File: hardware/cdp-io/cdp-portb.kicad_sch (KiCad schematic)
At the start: 5 parts, among them U1 74LS573, U2 74LS573, U7 74LS00

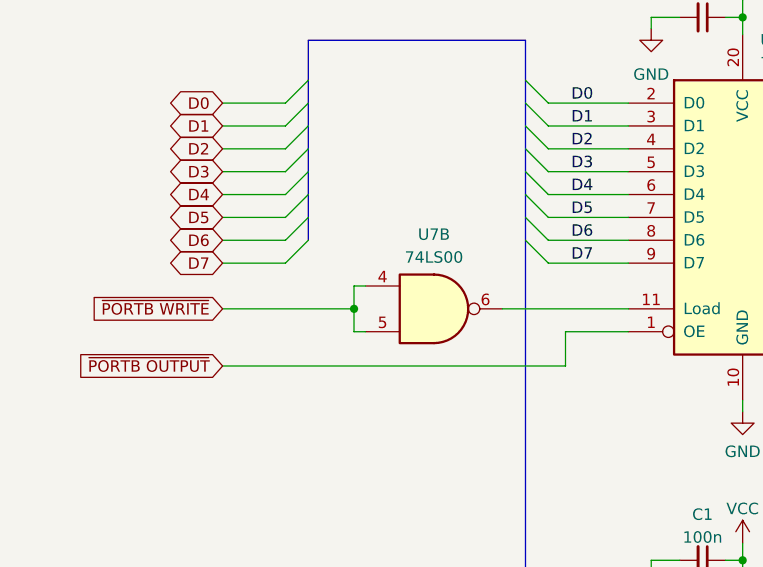
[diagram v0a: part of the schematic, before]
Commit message: The controller is finished. U7 is changed to a hex inverter.
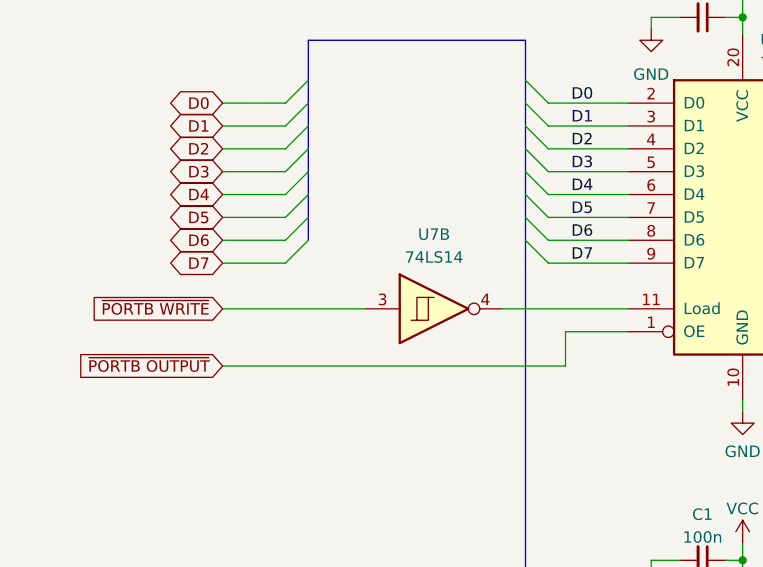
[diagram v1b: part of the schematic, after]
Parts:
- removed U7: 74LS00, Package_DIP:DIP-14_W7.62mm_Socket, symbol 74xx:74LS00
- added U7: 74LS14, symbol 74xx:74LS14
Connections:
- net ~{PORTB WRITE}: now also U7.3
- net at U1.11 (Load): now also U7.4
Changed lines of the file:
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@@
   (junction (at 155.575 93.345) (diameter 0) (color 0 0 0 0)
   )
-  (junction (at 112.395 65.405) (diameter 0) (color 0 0 0 0)
-  )
   (bus_entry (at 181.61 107.95) (size -2.54 2.54)
     (stroke (width 0) (type default))
@@
     (stroke (width 0) (type default))
   )
-  (wire (pts (xy 112.395 62.865) (xy 112.395 65.405))
-    (stroke (width 0) (type default))
-  )
   (wire (pts (xy 168.275 50.165) (xy 179.07 50.165))
     (stroke (width 0) (type default))
@@
     (stroke (width 0) (type default))
   )
-  (wire (pts (xy 112.395 65.405) (xy 112.395 67.945))
-    (stroke (width 0) (type default))
-  )
   (bus (pts (xy 206.375 55.245) (xy 206.375 57.785))
     (stroke (width 0) (type default))
@@
     (stroke (width 0) (type default))
   )
-  (wire (pts (xy 97.79 65.405) (xy 112.395 65.405))
+  (wire (pts (xy 97.79 65.405) (xy 113.665 65.405))
     (stroke (width 0) (type default))
   )
@@
     (stroke (width 0) (type default))
   )
-  (wire (pts (xy 112.395 67.945) (xy 113.665 67.945))
-    (stroke (width 0) (type default))
-  )
   (bus (pts (xy 181.61 42.545) (xy 181.61 40.005))
     (stroke (width 0) (type default))
@@
   )
   (wire (pts (xy 208.915 50.165) (xy 216.535 50.165))
-    (stroke (width 0) (type default))
-  )
-  (wire (pts (xy 113.665 62.865) (xy 112.395 62.865))
     (stroke (width 0) (type default))
   )
@@
     )
   )
-  (symbol (lib_id "74xx:74LS00") (at 121.285 65.405 0) (unit 2)
+  (symbol (lib_id "74xx:74LS14") (at 121.285 65.405 0) (unit 2)
     (in_bom yes) (on_board yes) (dnp no) (fields_autoplaced)
-    (property "Reference" "U7" (at 121.2767 57.15 0)
+    (property "Reference" "U7" (at 121.285 57.15 0)
       (effects (font (size 1.27 1.27)))
     )
-    (property "Value" "74LS00" (at 121.2767 59.69 0)
+    (property "Value" "74LS14" (at 121.285 59.69 0)
       (effects (font (size 1.27 1.27)))
     )
-    (property "Footprint" "Package_DIP:DIP-14_W7.62mm_Socket" (at 121.285 65.405 0)
-      (effects (font (size 1.27 1.27)) hide)
-    )
-    (property "Datasheet" "http://www.ti.com/lit/gpn/sn74ls00" (at 121.285 65.405 0)
+    (property "Footprint" "" (at 121.285 65.405 0)
+      (effects (font (size 1.27 1.27)) hide)
+    )
+    (property "Datasheet" "http://www.ti.com/lit/gpn/sn74LS14" (at 121.285 65.405 0)
       (effects (font (size 1.27 1.27)) hide)
     )
@@
     (pin "5")
     (pin "6")
-    (pin "10")
     (pin "8")
     (pin "9")
+    (pin "10")
     (pin "11")
     (pin "12")
@@
     (instances
       (project "cdp-io"
+        (path "/479e9a3e-8705-41df-8009-7e8503809f49/fc5dd19a-450f-4ce7-af21-025e7154e993"
+          (reference "U7") (unit 2)
+        )
         (path "/479e9a3e-8705-41df-8009-7e8503809f49/f2f2e87f-81b0-49e1-b285-4bb1f98f04a0"
           (reference "U7") (unit 2)

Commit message: Changed the layout a bit, started to work on the PCB.
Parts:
- U7: footprint (none) -> Package_DIP:DIP-14_W7.62mm_Socket
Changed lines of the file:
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@@
       (effects (font (size 1.27 1.27)))
     )
-    (property "Footprint" "" (at 121.285 65.405 0)
+    (property "Footprint" "Package_DIP:DIP-14_W7.62mm_Socket" (at 121.285 65.405 0)
       (effects (font (size 1.27 1.27)) hide)
     )

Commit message: Changed the schematic a bit.
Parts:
- removed U7: 74LS14, Package_DIP:DIP-14_W7.62mm_Socket, symbol 74xx:74LS14
- added U7: 74LS14, Package_DIP:DIP-14_W7.62mm_Socket, symbol 74xx:74LS14
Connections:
- net ~{PORTB WRITE}: now also U7.11
- net at U1.11 (Load): now also U7.10

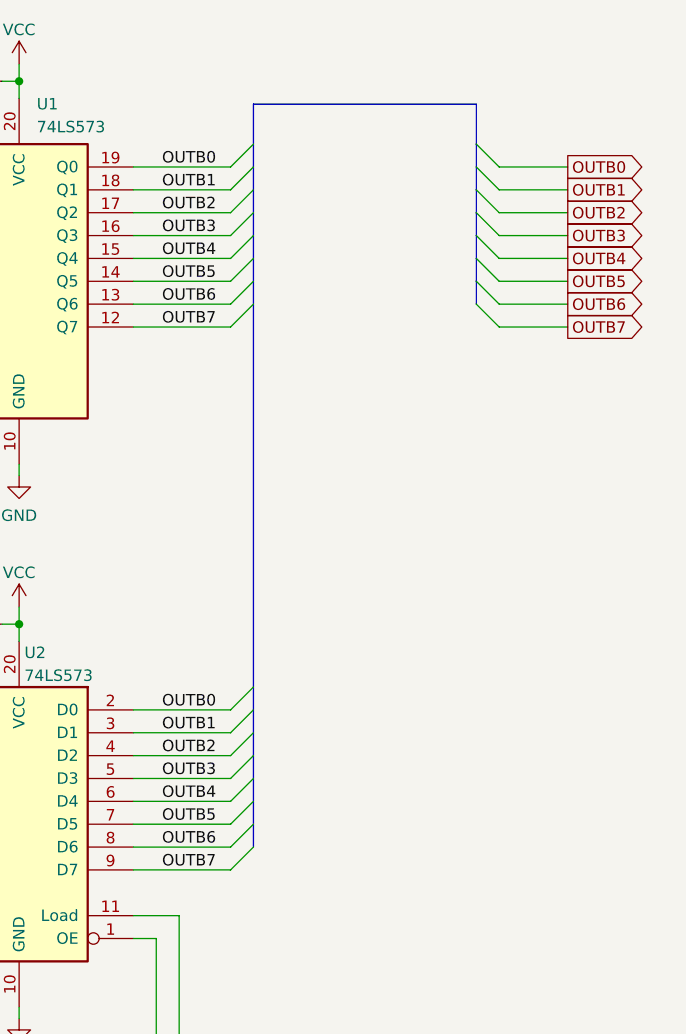
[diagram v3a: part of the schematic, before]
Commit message: Renamed a few net, and changed the schematic a bit. The PCB is ready!
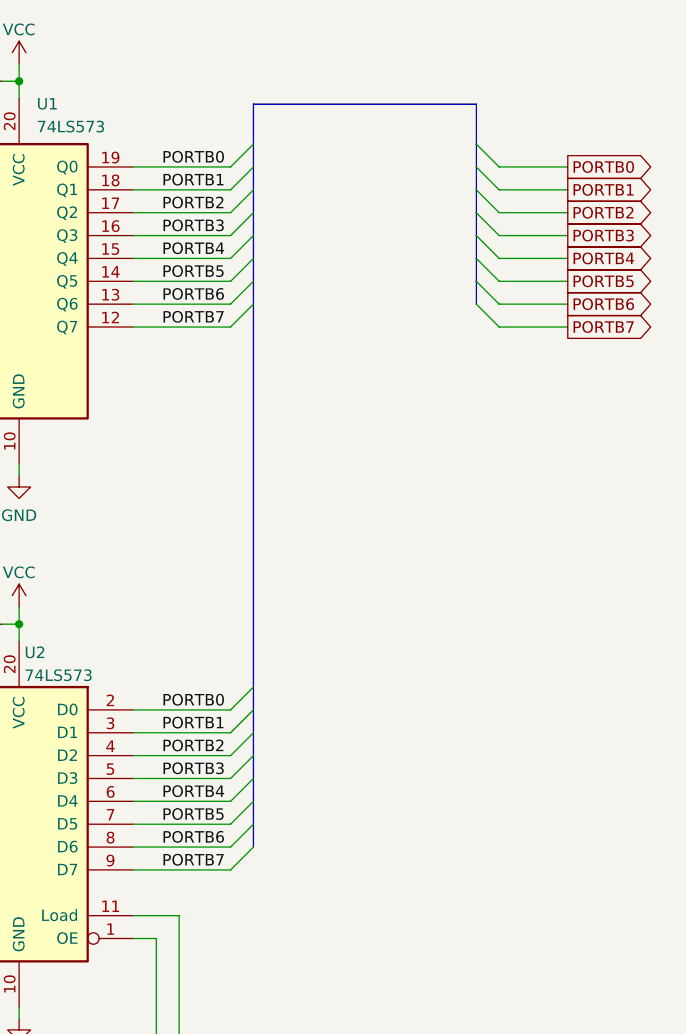
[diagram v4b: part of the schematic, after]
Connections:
- net OUTB0 renamed PORTB0
- net OUTB1 renamed PORTB1
- net OUTB2 renamed PORTB2
- net OUTB3 renamed PORTB3
- net OUTB4 renamed PORTB4
- net OUTB5 renamed PORTB5
- net OUTB6 renamed PORTB6
- net OUTB7 renamed PORTB7
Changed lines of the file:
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@@
     (effects (font (size 1.27 1.27)) (justify left bottom))
   )
-  (label "OUTB2" (at 171.45 47.625 0) (fields_autoplaced)
+  (label "PORTB2" (at 171.45 47.625 0) (fields_autoplaced)
     (effects (font (size 1.27 1.27)) (justify left bottom))
   )
-  (label "OUTB1" (at 171.45 45.085 0) (fields_autoplaced)
+  (label "PORTB1" (at 171.45 45.085 0) (fields_autoplaced)
     (effects (font (size 1.27 1.27)) (justify left bottom))
   )
-  (label "OUTB3" (at 171.45 110.49 0) (fields_autoplaced)
+  (label "PORTB3" (at 171.45 110.49 0) (fields_autoplaced)
     (effects (font (size 1.27 1.27)) (justify left bottom))
   )
@@
     (effects (font (size 1.27 1.27)) (justify left bottom))
   )
-  (label "OUTB7" (at 171.45 120.65 0) (fields_autoplaced)
+  (label "PORTB7" (at 171.45 120.65 0) (fields_autoplaced)
     (effects (font (size 1.27 1.27)) (justify left bottom))
   )
@@
     (effects (font (size 1.27 1.27)) (justify left bottom))
   )
-  (label "OUTB7" (at 171.45 60.325 0) (fields_autoplaced)
+  (label "PORTB7" (at 171.45 60.325 0) (fields_autoplaced)
     (effects (font (size 1.27 1.27)) (justify left bottom))
   )
-  (label "OUTB4" (at 171.45 52.705 0) (fields_autoplaced)
+  (label "PORTB4" (at 171.45 52.705 0) (fields_autoplaced)
     (effects (font (size 1.27 1.27)) (justify left bottom))
   )
-  (label "OUTB3" (at 171.45 50.165 0) (fields_autoplaced)
+  (label "PORTB3" (at 171.45 50.165 0) (fields_autoplaced)
     (effects (font (size 1.27 1.27)) (justify left bottom))
   )
-  (label "OUTB6" (at 171.45 57.785 0) (fields_autoplaced)
+  (label "PORTB6" (at 171.45 57.785 0) (fields_autoplaced)
     (effects (font (size 1.27 1.27)) (justify left bottom))
   )
-  (label "OUTB0" (at 171.45 102.87 0) (fields_autoplaced)
+  (label "PORTB0" (at 171.45 102.87 0) (fields_autoplaced)
     (effects (font (size 1.27 1.27)) (justify left bottom))
   )
@@
     (effects (font (size 1.27 1.27)) (justify left bottom))
   )
-  (label "OUTB2" (at 171.45 107.95 0) (fields_autoplaced)
+  (label "PORTB2" (at 171.45 107.95 0) (fields_autoplaced)
     (effects (font (size 1.27 1.27)) (justify left bottom))
   )
@@
     (effects (font (size 1.27 1.27)) (justify left bottom))
   )
-  (label "OUTB0" (at 171.45 42.545 0) (fields_autoplaced)
+  (label "PORTB0" (at 171.45 42.545 0) (fields_autoplaced)
     (effects (font (size 1.27 1.27)) (justify left bottom))
   )
@@
     (effects (font (size 1.27 1.27)) (justify left bottom))
   )
-  (label "OUTB5" (at 171.45 115.57 0) (fields_autoplaced)
+  (label "PORTB5" (at 171.45 115.57 0) (fields_autoplaced)
     (effects (font (size 1.27 1.27)) (justify left bottom))
   )
@@
     (effects (font (size 1.27 1.27)) (justify left bottom))
   )
-  (label "OUTB1" (at 171.45 105.41 0) (fields_autoplaced)
+  (label "PORTB1" (at 171.45 105.41 0) (fields_autoplaced)
     (effects (font (size 1.27 1.27)) (justify left bottom))
   )
-  (label "OUTB6" (at 171.45 118.11 0) (fields_autoplaced)
+  (label "PORTB6" (at 171.45 118.11 0) (fields_autoplaced)
     (effects (font (size 1.27 1.27)) (justify left bottom))
   )
-  (label "OUTB5" (at 171.45 55.245 0) (fields_autoplaced)
+  (label "PORTB5" (at 171.45 55.245 0) (fields_autoplaced)
     (effects (font (size 1.27 1.27)) (justify left bottom))
   )
-  (label "OUTB4" (at 171.45 113.03 0) (fields_autoplaced)
+  (label "PORTB4" (at 171.45 113.03 0) (fields_autoplaced)
     (effects (font (size 1.27 1.27)) (justify left bottom))
   )
-  (global_label "OUTB5" (shape output) (at 216.535 55.245 0) (fields_autoplaced)
+  (global_label "PORTB5" (shape output) (at 216.535 55.245 0) (fields_autoplaced)
     (effects (font (size 1.27 1.27)) (justify left))
-    (property "Intersheetrefs" "${INTERSHEET_REFS}" (at 225.5489 55.245 0)
+    (property "Intersheetrefs" "${INTERSHEET_REFS}" (at 226.7584 55.245 0)
       (effects (font (size 1.27 1.27)) (justify left) hide)
     )
@@
     )
   )
-  (global_label "OUTB3" (shape output) (at 216.535 50.165 0) (fields_autoplaced)
+  (global_label "PORTB3" (shape output) (at 216.535 50.165 0) (fields_autoplaced)
     (effects (font (size 1.27 1.27)) (justify left))
-    (property "Intersheetrefs" "${INTERSHEET_REFS}" (at 225.5489 50.165 0)
+    (property "Intersheetrefs" "${INTERSHEET_REFS}" (at 226.7584 50.165 0)
       (effects (font (size 1.27 1.27)) (justify left) hide)
     )
@@
     )
   )
-  (global_label "OUTB0" (shape output) (at 216.535 42.545 0) (fields_autoplaced)
+  (global_label "PORTB0" (shape output) (at 216.535 42.545 0) (fields_autoplaced)
     (effects (font (size 1.27 1.27)) (justify left))
-    (property "Intersheetrefs" "${INTERSHEET_REFS}" (at 225.5489 42.545 0)
+    (property "Intersheetrefs" "${INTERSHEET_REFS}" (at 226.7584 42.545 0)
       (effects (font (size 1.27 1.27)) (justify left) hide)
     )
@@
     )
   )
-  (global_label "OUTB6" (shape output) (at 216.535 57.785 0) (fields_autoplaced)
+  (global_label "PORTB6" (shape output) (at 216.535 57.785 0) (fields_autoplaced)
     (effects (font (size 1.27 1.27)) (justify left))
-    (property "Intersheetrefs" "${INTERSHEET_REFS}" (at 225.5489 57.785 0)
+    (property "Intersheetrefs" "${INTERSHEET_REFS}" (at 226.7584 57.785 0)
       (effects (font (size 1.27 1.27)) (justify left) hide)
     )
   )
-  (global_label "OUTB4" (shape output) (at 216.535 52.705 0) (fields_autoplaced)
+  (global_label "PORTB4" (shape output) (at 216.535 52.705 0) (fields_autoplaced)
     (effects (font (size 1.27 1.27)) (justify left))
-    (property "Intersheetrefs" "${INTERSHEET_REFS}" (at 225.5489 52.705 0)
+    (property "Intersheetrefs" "${INTERSHEET_REFS}" (at 226.7584 52.705 0)
       (effects (font (size 1.27 1.27)) (justify left) hide)
     )
   )
-  (global_label "OUTB7" (shape output) (at 216.535 60.325 0) (fields_autoplaced)
+  (global_label "PORTB7" (shape output) (at 216.535 60.325 0) (fields_autoplaced)
     (effects (font (size 1.27 1.27)) (justify left))
-    (property "Intersheetrefs" "${INTERSHEET_REFS}" (at 225.5489 60.325 0)
+    (property "Intersheetrefs" "${INTERSHEET_REFS}" (at 226.7584 60.325 0)
       (effects (font (size 1.27 1.27)) (justify left) hide)
     )
@@
     )
   )
-  (global_label "OUTB2" (shape output) (at 216.535 47.625 0) (fields_autoplaced)
+  (global_label "PORTB2" (shape output) (at 216.535 47.625 0) (fields_autoplaced)
     (effects (font (size 1.27 1.27)) (justify left))
-    (property "Intersheetrefs" "${INTERSHEET_REFS}" (at 225.5489 47.625 0)
+    (property "Intersheetrefs" "${INTERSHEET_REFS}" (at 226.7584 47.625 0)
       (effects (font (size 1.27 1.27)) (justify left) hide)
     )
   )
-  (global_label "OUTB1" (shape output) (at 216.535 45.085 0) (fields_autoplaced)
+  (global_label "PORTB1" (shape output) (at 216.535 45.085 0) (fields_autoplaced)
     (effects (font (size 1.27 1.27)) (justify left))
-    (property "Intersheetrefs" "${INTERSHEET_REFS}" (at 225.5489 45.085 0)
+    (property "Intersheetrefs" "${INTERSHEET_REFS}" (at 226.7584 45.085 0)
       (effects (font (size 1.27 1.27)) (justify left) hide)
     )

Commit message: The final version of the IO board. Gerber files added.
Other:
- company: (none) -> ZLED
- title: (none) -> Port B
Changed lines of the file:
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@@
 (kicad_sch (version 20230121) (generator eeschema)
   (paper "A4")
+  (title_block
+    (title "Port B")
+    (date "2023-07-06")
+    (rev "1")
+    (company "ZLED")
+  )
   (junction (at 155.575 33.02) (diameter 0) (color 0 0 0 0)
   )

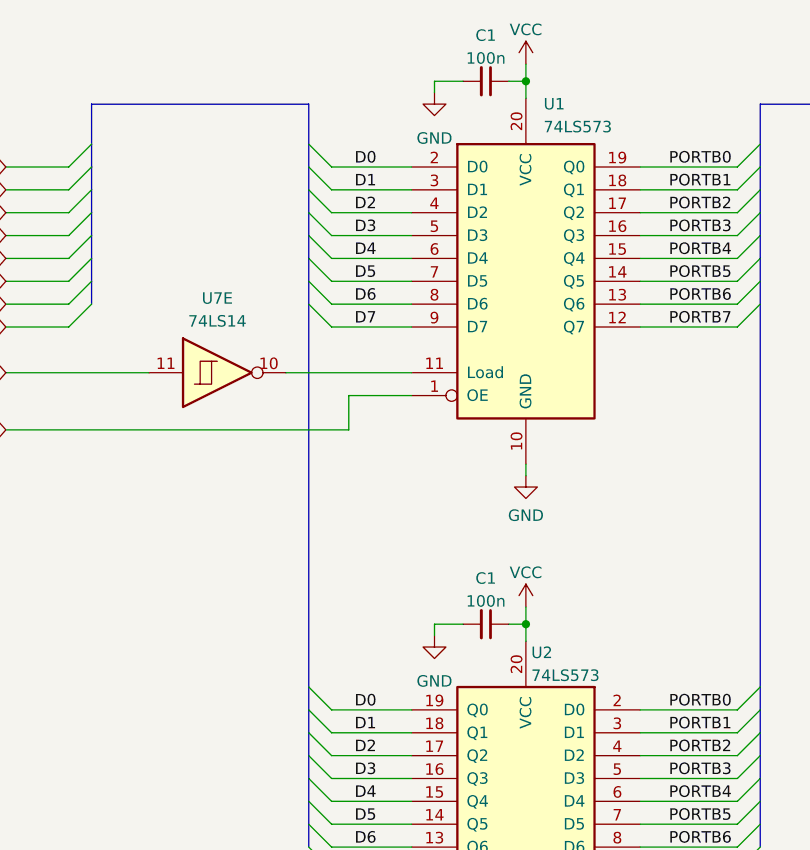
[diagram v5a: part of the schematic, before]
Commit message: IC names fixed. PCB is updated. Gerber files are still ok.
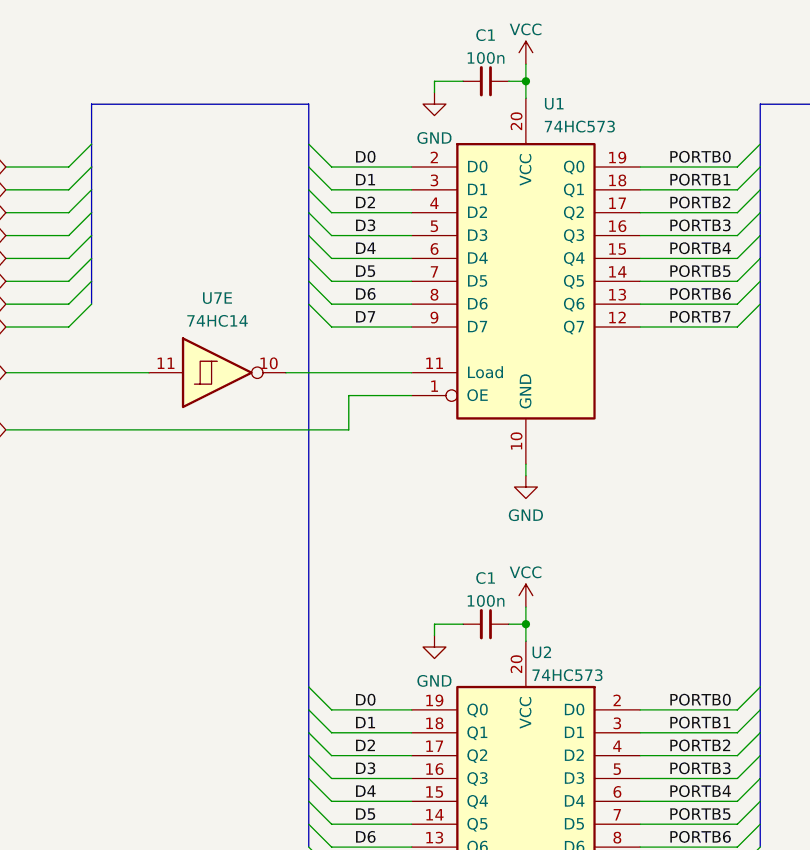
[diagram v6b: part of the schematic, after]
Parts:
- U1, U2: value 74LS573 -> 74HC573
- U7: value 74LS14 -> 74HC14
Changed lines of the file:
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@@
       (effects (font (size 1.27 1.27)) (justify left))
     )
-    (property "Value" "74LS573" (at 157.5309 38.1 0)
+    (property "Value" "74HC573" (at 157.5309 38.1 0)
       (effects (font (size 1.27 1.27)) (justify left))
     )
@@
       (effects (font (size 1.27 1.27)))
     )
-    (property "Value" "74LS14" (at 121.285 59.69 0)
+    (property "Value" "74HC14" (at 121.285 59.69 0)
       (effects (font (size 1.27 1.27)))
     )
@@
       (effects (font (size 1.27 1.27)) (justify right))
     )
-    (property "Value" "74LS573" (at 156.1591 99.06 0)
+    (property "Value" "74HC573" (at 156.1591 99.06 0)
       (effects (font (size 1.27 1.27)) (justify right))
     )
